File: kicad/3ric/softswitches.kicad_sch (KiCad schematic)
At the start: 11 parts

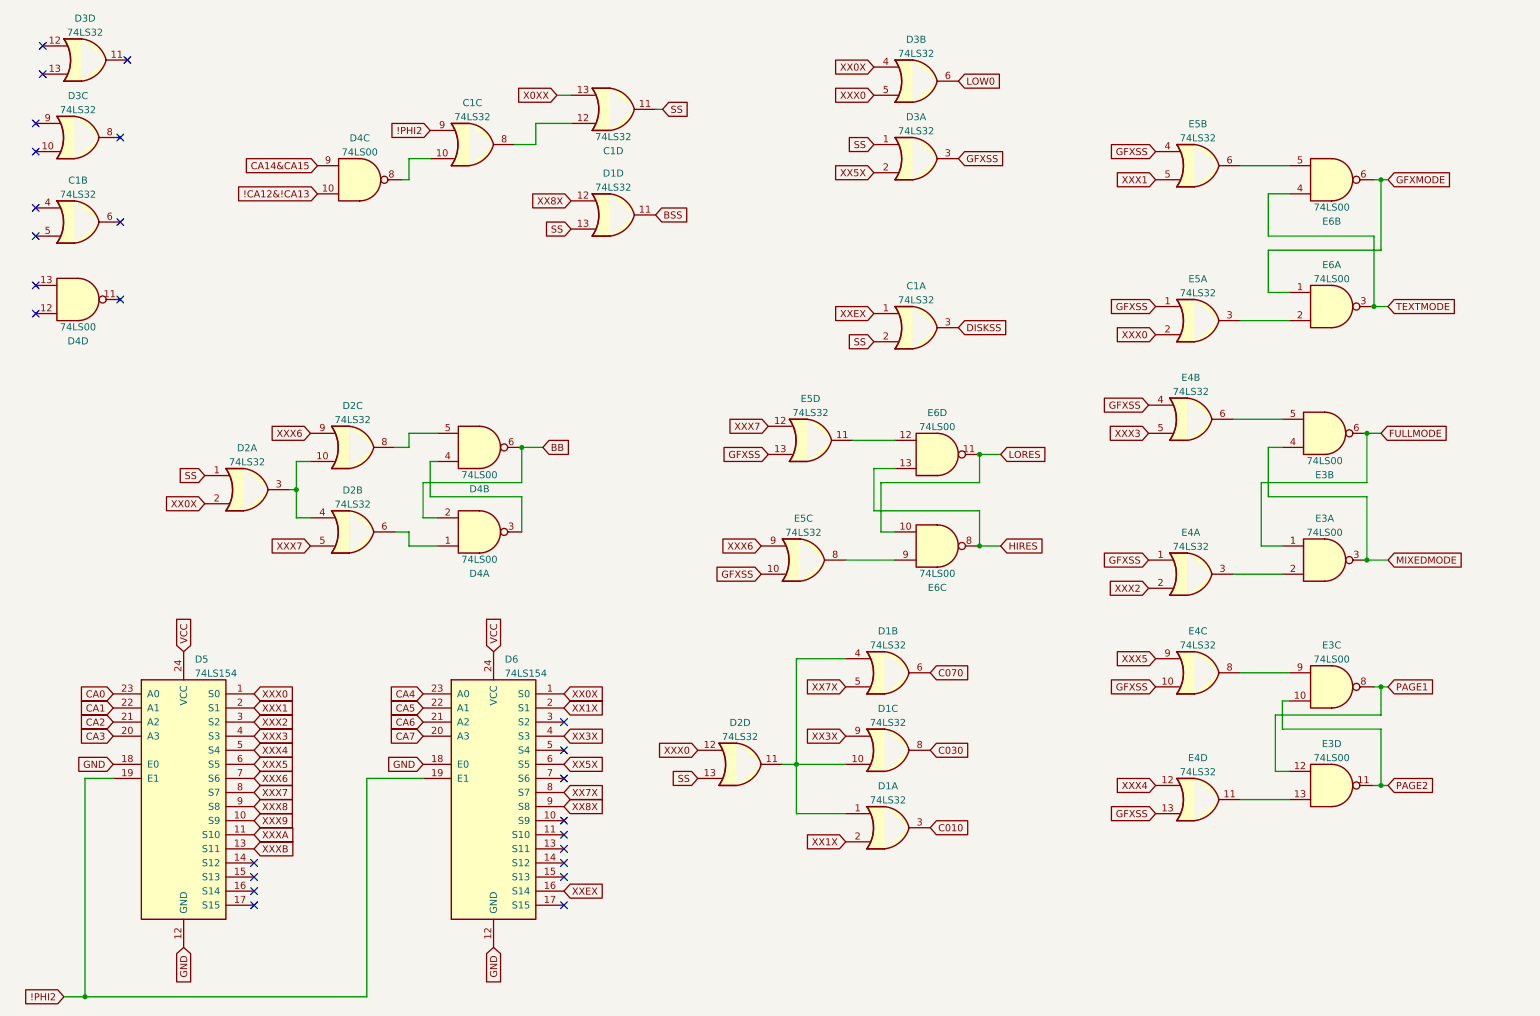
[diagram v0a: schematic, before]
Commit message: updated schematics and PCB PNG of the breadboard layout
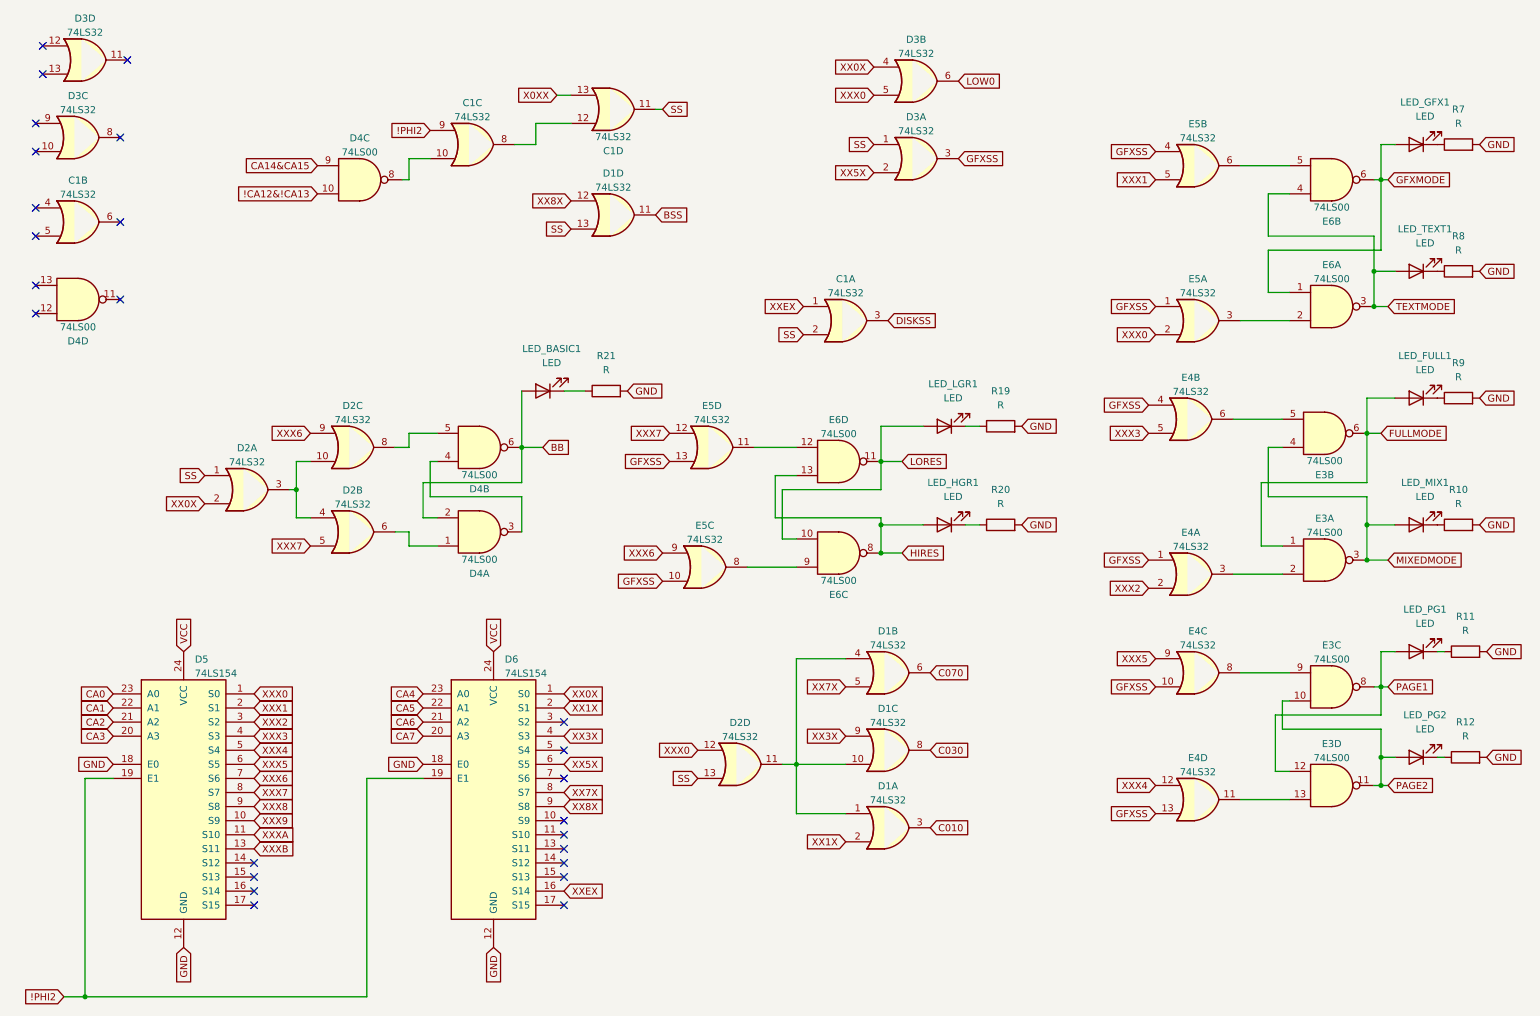
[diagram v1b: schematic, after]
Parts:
- added LED_BASIC1, LED_FULL1, LED_GFX1, LED_HGR1, LED_LGR1, LED_MIX1, LED_PG1, LED_PG2, LED_TEXT1: LED, LED_THT:LED_D5.0mm, symbol Device:LED
- added R10, R11, R12, R19, R20, R21, R7, R8, R9: R, Resistor_SMD:R_0603_1608Metric_Pad0.98x0.95mm_HandSolder, symbol Device:R
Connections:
- net BB: now also LED_BASIC1.2 (A)
- net FULLMODE: now also LED_FULL1.2 (A)
- net GFXMODE: now also LED_GFX1.2 (A)
- net GND: now also R10.2, R11.2, R12.2, R19.2, R20.2, R21.2, R7.2, R8.2, R9.2
- net HIRES: now also LED_HGR1.2 (A)
- net LORES: now also LED_LGR1.2 (A)
- net MIXEDMODE: now also LED_MIX1.2 (A)
- net PAGE1: now also LED_PG1.2 (A)
- net PAGE2: now also LED_PG2.2 (A)
- net TEXTMODE: now also LED_TEXT1.2 (A)
- new net: LED_PG2.1 (K), R12.1
- new net: LED_MIX1.1 (K), R10.1
- new net: LED_GFX1.1 (K), R7.1
- new net: LED_BASIC1.1 (K), R21.1
- new net: LED_PG1.1 (K), R11.1
- new net: LED_LGR1.1 (K), R19.1
- new net: LED_HGR1.1 (K), R20.1
- new net: LED_TEXT1.1 (K), R8.1
- new net: LED_FULL1.1 (K), R9.1
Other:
- moved on the sheet: C1A, E5C, E5D, E6C, E6D

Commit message: pcb layout continued
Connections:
- net LOW0: no longer names the net of D3.6
- no-connect marks 25 -> 26
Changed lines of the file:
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@@
+	)
+	(no_connect
+		(at 182.88 25.4)
 	)
 	(no_connect
@@
 				(hide yes)
 			)
-		)
-	)
-	(global_label "LOW0"
-		(shape input)
-		(at 182.88 25.4 0)
-		(fields_autoplaced yes)
-		(effects
-			(font
-				(size 1.27 1.27)
-			)
-			(justify left)
-		)
-		(property "Intersheetrefs" "${INTERSHEET_REFS}"
-			(at 190.3126 25.3206 0)
-			(effects
-				(font
-					(size 1.27 1.27)
-				)
-				(justify left)
-				(hide yes)
-			)

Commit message: v2 pcb
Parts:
- R10, R11, R12, R19, R20, R21, R7, R8, R9: value R -> R220
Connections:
- net XX0X: no longer D3.4
- net XXX0: no longer D3.5
- no-connect marks 26 -> 28
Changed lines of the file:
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@@
 	)
 	(no_connect
+		(at 167.64 22.86)
+	)
+	(no_connect
 		(at 31.75 50.8)
 	)
@@
 	)
 	(no_connect
+		(at 167.64 27.94)
+	)
+	(no_connect
 		(at 55.88 166.37)
 	)
@@
 		)
 	)
-	(global_label "XX0X"
-		(shape input)
-		(at 167.64 22.86 180)
-		(fields_autoplaced yes)
-		(effects
-			(font
-				(size 1.27 1.27)
-			)
-			(justify right)
-		)
-		(property "Intersheetrefs" "${INTERSHEET_REFS}"
-			(at 159.8168 22.86 0)
-			(effects
-				(font
-					(size 1.27 1.27)
-				)
-				(justify right)
-				(hide yes)
-			)
-		)
-	)
 	(global_label "CA2"
 		(shape input)
@@
 		)
 	)
-	(global_label "XXX0"
-		(shape input)
-		(at 167.64 27.94 180)
-		(fields_autoplaced yes)
-		(effects
-			(font
-				(size 1.27 1.27)
-			)
-			(justify right)
-		)
-		(property "Intersheetrefs" "${INTERSHEET_REFS}"
-			(at 160.3888 27.8606 0)
-			(effects
-				(font
-					(size 1.27 1.27)
-				)
-				(justify right)
-				(hide yes)
-			)
-		)
-	)
 	(global_label "XXX3"
 		(shape input)
@@
 			)
 		)
-		(property "Value" "R"
+		(property "Value" "R220"
 			(at 274.32 143.51 90)
 			(effects
@@
 			)
 		)
-		(property "Value" "R"
+		(property "Value" "R220"
 			(at 273.05 33.02 90)
 			(effects
@@
 			)
 		)
-		(property "Value" "R"
+		(property "Value" "R220"
 			(at 274.32 124.46 90)
 			(effects
@@
 			)
 		)
-		(property "Value" "R"
+		(property "Value" "R220"
 			(at 190.5 83.82 90)
 			(effects
@@
 			)
 		)
-		(property "Value" "R"
+		(property "Value" "R220"
 			(at 273.05 101.6 90)
 			(effects
@@
 			)
 		)
-		(property "Value" "R"
+		(property "Value" "R220"
 			(at 190.5 101.6 90)
 			(effects
@@
 			)
 		)
-		(property "Value" "R"
+		(property "Value" "R220"
 			(at 273.05 55.88 90)
 			(effects
@@
 			)
 		)
-		(property "Value" "R"
+		(property "Value" "R220"
 			(at 273.05 78.74 90)
 			(effects
@@
 			)
 		)
-		(property "Value" "R"
+		(property "Value" "R220"
 			(at 119.38 77.47 90)
 			(effects
